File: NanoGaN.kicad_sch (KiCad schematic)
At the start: 11 parts, among them J1 U_DC, J2 GND, J3 Phase_U, J4 Phase_V, J5 Phase_W

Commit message: WiP layout
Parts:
- removed H1, H2, H3, H4, H5, H6: MountingHole, MountingHole:MountingHole_3.2mm_M3, symbol Mechanical:MountingHole
- added FM1, FM2, FM3: Fiducial, Fiducial:Fiducial_1mm_Mask2mm, symbol Mechanical:Fiducial
- added MH1, MH2, MH3, MH4, MH5, MH6: M2, MountingHole:MountingHole_2.2mm_M2_Pad_Via, symbol Mechanical:MountingHole_Pad
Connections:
- new net GND: MH1.1, MH2.1, MH3.1, MH4.1, MH5.1, MH6.1
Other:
- sheet Connectors ports: added SERVO; removed none
- sheet MCU ports: added SERVO; removed none

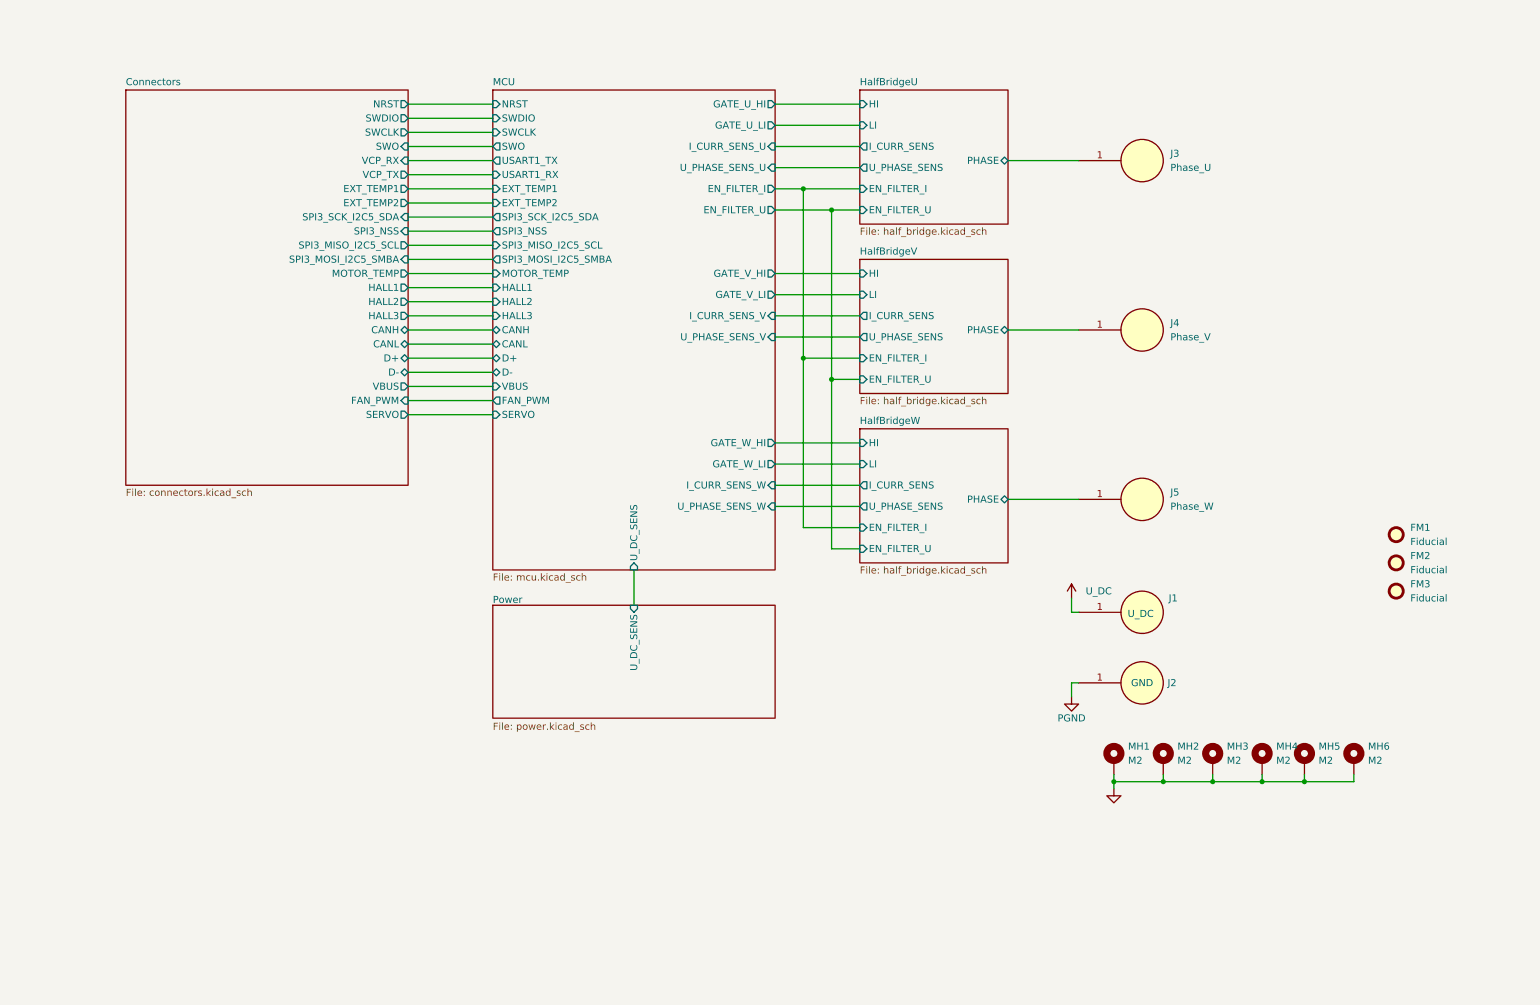
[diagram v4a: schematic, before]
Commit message: added over current protection triggers (adjustable)
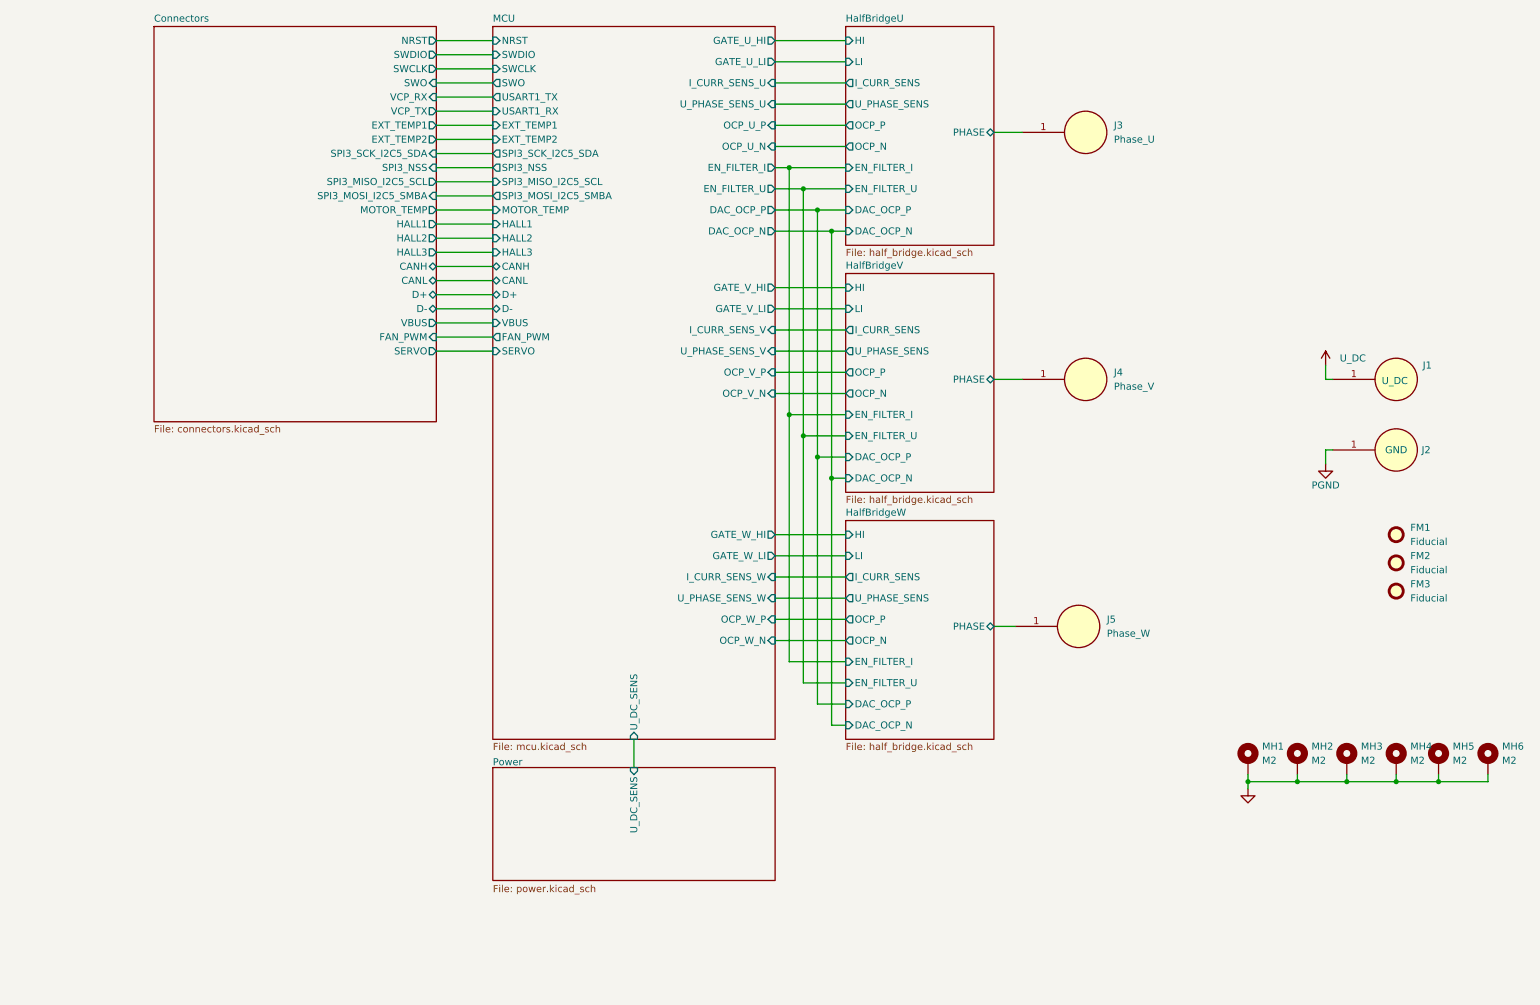
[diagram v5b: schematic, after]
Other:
- sheet HalfBridgeU ports: added DAC_OCP_N, DAC_OCP_P, OCP_N, OCP_P; removed none
- sheet HalfBridgeV ports: added DAC_OCP_N, DAC_OCP_P, OCP_N, OCP_P; removed none
- sheet HalfBridgeW ports: added DAC_OCP_N, DAC_OCP_P, OCP_N, OCP_P; removed none
- sheet MCU ports: added DAC_OCP_N, DAC_OCP_P, OCP_U_N, OCP_U_P, OCP_V_N, OCP_V_P, OCP_W_N, OCP_W_P; removed none
- moved on the sheet: J1, J2, J3, J4, J5, MH1, MH2, MH3, MH4, MH5, MH6

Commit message: WiP layout
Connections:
- net GND: no longer MH3.1, MH4.1, MH5.1, MH6.1
- net PGND: now also MH3.1, MH4.1, MH5.1, MH6.1
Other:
- sheet Connectors ports: added none; removed VBUS
- sheet MCU ports: added none; removed VBUS
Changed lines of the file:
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@@
+	)
+	(junction
+		(at 160.02 58.42)
+		(diameter 0)
+		(color 0 0 0 0)
+	)
+	(junction
+		(at 157.48 99.06)
+		(diameter 0)
+		(color 0 0 0 0)
+	)
+	(junction
+		(at 152.4 91.44)
+		(diameter 0)
+		(color 0 0 0 0)
+	)
+	(junction
+		(at 154.94 95.25)
+		(diameter 0)
+		(color 0 0 0 0)
 	)
 	(junction
@@
 	)
 	(junction
-		(at 160.02 58.42)
-		(diameter 0)
-		(color 0 0 0 0)
-	)
-	(junction
-		(at 157.48 99.06)
-		(diameter 0)
-		(color 0 0 0 0)
-	)
-	(junction
-		(at 152.4 91.44)
-		(diameter 0)
-		(color 0 0 0 0)
-	)
-	(junction
-		(at 154.94 95.25)
-		(diameter 0)
-		(color 0 0 0 0)
-	)
-	(junction
 		(at 269.24 157.48)
 		(diameter 0)
@@
 		(color 0 0 0 0)
 	)
-	(junction
-		(at 243.84 157.48)
-		(diameter 0)
-		(color 0 0 0 0)
-	)
 	(wire
 		(pts
@@
 	(wire
 		(pts
+			(xy 88.9 74.93) (xy 99.06 74.93)
+		)
+		(stroke
+			(width 0)
+			(type default)
+		)
+	)
+	(wire
+		(pts
 			(xy 88.9 72.39) (xy 99.06 72.39)
 		)
@@
 	(wire
 		(pts
-			(xy 88.9 80.01) (xy 99.06 80.01)
+			(xy 88.9 77.47) (xy 99.06 77.47)
 		)
 		(stroke
@@
 	(wire
 		(pts
-			(xy 88.9 77.47) (xy 99.06 77.47)
-		)
-		(stroke
-			(width 0)
-			(type default)
-		)
-	)
-	(wire
-		(pts
 			(xy 149.86 27.94) (xy 162.56 27.94)
 		)
@@
 	(wire
 		(pts
+			(xy 252.73 157.48) (xy 252.73 158.75)
+		)
+		(stroke
+			(width 0)
+			(type default)
+		)
+	)
+	(wire
+		(pts
 			(xy 162.56 99.06) (xy 157.48 99.06)
 		)
@@
 	(wire
 		(pts
-			(xy 88.9 74.93) (xy 99.06 74.93)
-		)
-		(stroke
-			(width 0)
-			(type default)
-		)
-	)
-	(wire
-		(pts
 			(xy 160.02 147.32) (xy 160.02 102.87)
 		)
@@
 		(pts
 			(xy 248.92 97.79) (xy 248.92 100.33)
-		)
-		(stroke
-			(width 0)
-			(type default)
-		)
-	)
-	(wire
-		(pts
-			(xy 252.73 157.48) (xy 243.84 157.48)
 		)
 		(stroke
@@
 					(size 1.27 1.27)
 				)
-				(hide yes)
 			)
 		)
@@
 				(path "/aa8a494f-605e-4a00-9d3c-daec94709fcb"
 					(reference "#PWR0131")
+					(unit 1)
+				)
+			)
+		)
+	)
+	(symbol
+		(lib_id "power:GND")
+		(at 252.73 158.75 0)
+		(unit 1)
+		(exclude_from_sim no)
+		(in_bom yes)
+		(on_board yes)
+		(dnp no)
+		(property "Reference" "#PWR0111"
+			(at 252.73 165.1 0)
+			(effects
+				(font
+					(size 1.27 1.27)
+				)
+				(hide yes)
+			)
+		)
+		(property "Value" "PGND"
+			(at 252.73 162.814 0)
+			(effects
+				(font
+					(size 1.27 1.27)
+				)
+			)
+		)
+		(property "Footprint" ""
+			(at 252.73 158.75 0)
+			(effects
+				(font
+					(size 1.27 1.27)
+				)
+				(hide yes)
+			)
+		)
+		(property "Datasheet" ""
+			(at 252.73 158.75 0)
+			(effects
+				(font
+					(size 1.27 1.27)
+				)
+				(hide yes)
+			)
+		)
+		(property "Description" "Power symbol creates a global label with name \"GND\" , ground"
+			(at 252.73 158.75 0)
+			(effects
+				(font
+					(size 1.27 1.27)
+				)
+				(hide yes)
+			)
+		)
+		(pin "1"
+		)
+		(instances
+			(project "NanoGaN"
+				(path "/aa8a494f-605e-4a00-9d3c-daec94709fcb"
+					(reference "#PWR0111")
 					(unit 1)
 				)
@@
 			)
 		)
-		(pin "VBUS" output
-			(at 88.9 74.93 0)
-			(effects
-				(font
-					(size 1.27 1.27)
-				)
-				(justify right)
-			)
-		)
 		(pin "EXT_TEMP1" output
 			(at 88.9 39.37 0)
@@
 		)
 		(pin "FAN_PWM" input
+			(at 88.9 74.93 0)
+			(effects
+				(font
+					(size 1.27 1.27)
+				)
+				(justify right)
+			)
+		)
+		(pin "SERVO" output
 			(at 88.9 77.47 0)
-			(effects
-				(font
-					(size 1.27 1.27)
-				)
-				(justify right)
-			)
-		)
-		(pin "SERVO" output
-			(at 88.9 80.01 0)
 			(effects
 				(font
@@
 			)
 		)
-		(pin "VBUS" input
-			(at 99.06 74.93 180)
-			(effects
-				(font
-					(size 1.27 1.27)
-				)
-				(justify left)
-			)
-		)
 		(pin "D-" bidirectional
 			(at 99.06 72.39 180)
@@
 		)
 		(pin "FAN_PWM" output
+			(at 99.06 74.93 180)
+			(effects
+				(font
+					(size 1.27 1.27)
+				)
+				(justify left)
+			)
+		)
+		(pin "SERVO" input
 			(at 99.06 77.47 180)
 			(effects
 				(font
-					(size 1.27 1.27)
-				)
-				(justify left)
-			)
-		)
-		(pin "SERVO" input
-			(at 99.06 80.01 180)
-			(effects
-				(font

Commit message: added the first draft of the layout
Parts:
- removed J1: U_DC, TerminalBlock_Wuerth:Wuerth_REDCUBE-THR_WP-THRBU_74650073_THR, symbol Connector_Generic:Power_Welding_PAD
- removed J2: GND, TerminalBlock_Wuerth:Wuerth_REDCUBE-THR_WP-THRBU_74650073_THR, symbol Connector_Generic:Power_Welding_PAD
- added CC1: ~, NanoGaN:CoolingChannel, symbol NanoGaN:CoolingChannel
- added J1, J2: XT60-M, NanoGaN:AMASS_XT60-M, symbol NanoGaN:XT60-M
- added MH7: M3, MountingHole:MountingHole_3.2mm_M3_Pad_Via, symbol Mechanical:MountingHole_Pad
- MH1, MH2, MH3, MH4, MH5, MH6: value M2 -> M3; footprint MountingHole:MountingHole_2.2mm_M2_Pad_Via -> MountingHole:MountingHole_3.2mm_M3_Pad_Via
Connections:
- net GND: now also MH3.1
- net PGND: now also J1.N (NEG), J2.N (NEG), MH7.1; no longer MH3.1
- net U_DC: now also J1.P (POS), J2.P (POS)
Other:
- sheet HalfBridgeU ports: added I_CURR_SENS+, I_CURR_SENS-; removed EN_FILTER_I, EN_FILTER_U, I_CURR_SENS
- sheet HalfBridgeV ports: added I_CURR_SENS+, I_CURR_SENS-; removed EN_FILTER_I, EN_FILTER_U, I_CURR_SENS
- sheet HalfBridgeW ports: added I_CURR_SENS+, I_CURR_SENS-; removed EN_FILTER_I, EN_FILTER_U, I_CURR_SENS
- sheet MCU ports: added I_CURR_SENS_U+, I_CURR_SENS_U-, I_CURR_SENS_V+, I_CURR_SENS_V-, I_CURR_SENS_W+, I_CURR_SENS_W-; removed EN_FILTER_I, EN_FILTER_U, I_CURR_SENS_U, I_CURR_SENS_V, I_CURR_SENS_W
- note added: "Mechanical Stuff (no BOM)"
- moved on the sheet: FM1, FM2, FM3, MH1

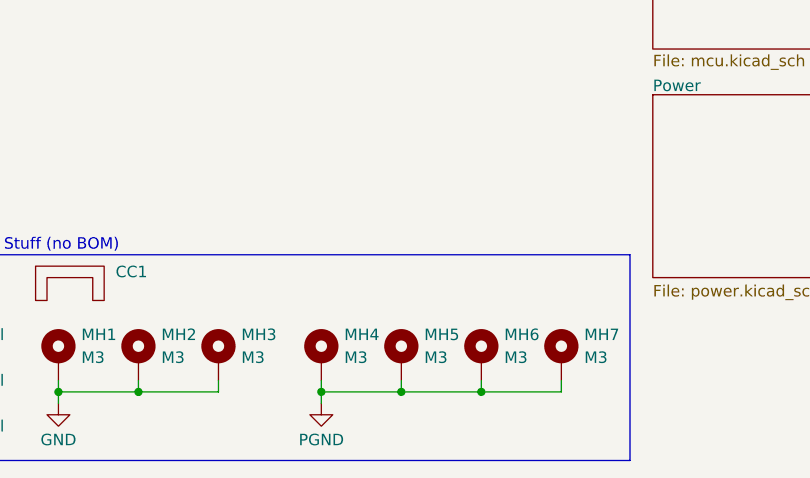
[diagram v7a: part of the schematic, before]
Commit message: added heatsinks and updated cooling channel
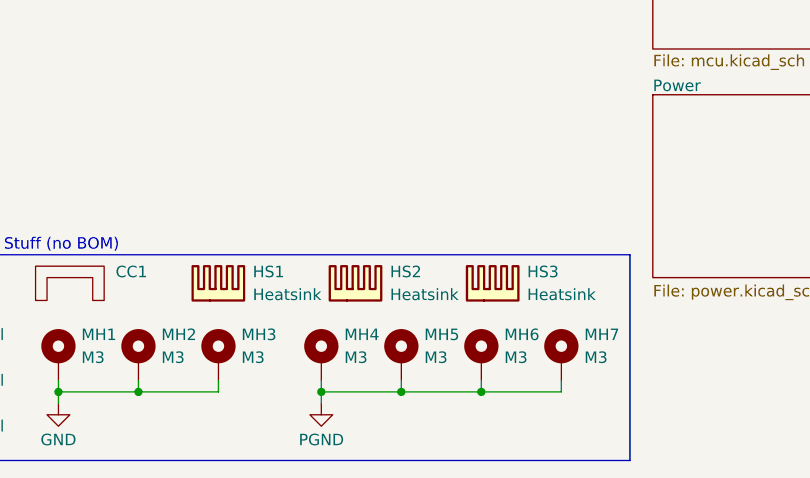
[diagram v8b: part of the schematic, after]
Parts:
- added HS1, HS2, HS3: Heatsink, NanoGaN:HSB01-080808, symbol Mechanical:Heatsink
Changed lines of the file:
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@@
+	)
+	(symbol
+		(lib_id "Mechanical:Heatsink")
+		(at 66.04 177.8 0)
+		(unit 1)
+		(exclude_from_sim no)
+		(in_bom yes)
+		(on_board yes)
+		(dnp no)
+		(fields_autoplaced yes)
+		(property "Reference" "HS2"
+			(at 69.85 174.6249 0)
+			(effects
+				(font
+					(size 1.27 1.27)
+				)
+				(justify left)
+			)
+		)
+		(property "Value" "Heatsink"
+			(at 69.85 177.1649 0)
+			(effects
+				(font
+					(size 1.27 1.27)
+				)
+				(justify left)
+			)
+		)
+		(property "Footprint" "NanoGaN:HSB01-080808"
+			(at 66.3448 177.8 0)
+			(effects
+				(font
+					(size 1.27 1.27)
+				)
+				(hide yes)
+			)
+		)
+		(property "Datasheet" "~"
+			(at 66.3448 177.8 0)
+			(effects
+				(font
+					(size 1.27 1.27)
+				)
+				(hide yes)
+			)
+		)
+		(property "Description" "Heatsink"
+			(at 66.04 177.8 0)
+			(effects
+				(font
+					(size 1.27 1.27)
+				)
+				(hide yes)
+			)
+		)
+		(instances
+			(project "NanoGaN"
+				(path "/aa8a494f-605e-4a00-9d3c-daec94709fcb"
+					(reference "HS2")
+					(unit 1)
+				)
+			)
+		)
+	)
+	(symbol
+		(lib_id "Mechanical:Heatsink")
+		(at 81.28 177.8 0)
+		(unit 1)
+		(exclude_from_sim no)
+		(in_bom yes)
+		(on_board yes)
+		(dnp no)
+		(fields_autoplaced yes)
+		(property "Reference" "HS3"
+			(at 85.09 174.6249 0)
+			(effects
+				(font
+					(size 1.27 1.27)
+				)
+				(justify left)
+			)
+		)
+		(property "Value" "Heatsink"
+			(at 85.09 177.1649 0)
+			(effects
+				(font
+					(size 1.27 1.27)
+				)
+				(justify left)
+			)
+		)
+		(property "Footprint" "NanoGaN:HSB01-080808"
+			(at 81.5848 177.8 0)
+			(effects
+				(font
+					(size 1.27 1.27)
+				)
+				(hide yes)
+			)
+		)
+		(property "Datasheet" "~"
+			(at 81.5848 177.8 0)
+			(effects
+				(font
+					(size 1.27 1.27)
+				)
+				(hide yes)
+			)
+		)
+		(property "Description" "Heatsink"
+			(at 81.28 177.8 0)
+			(effects
+				(font
+					(size 1.27 1.27)
+				)
+				(hide yes)
+			)
+		)
+		(instances
+			(project "NanoGaN"
+				(path "/aa8a494f-605e-4a00-9d3c-daec94709fcb"
+					(reference "HS3")
+					(unit 1)
+				)
+			)
+		)
 	)
 	(symbol
@@
 					(unit 1)
 				)
+			)
+		)
+	)
+	(symbol
+		(lib_id "Mechanical:Heatsink")
+		(at 50.8 177.8 0)
+		(unit 1)
+		(exclude_from_sim no)
+		(in_bom yes)
+		(on_board yes)
+		(dnp no)
+		(fields_autoplaced yes)
+		(property "Reference" "HS1"
+			(at 54.61 174.6249 0)
+			(effects
+				(font
+					(size 1.27 1.27)
+				)
+				(justify left)
+			)
+		)
+		(property "Value" "Heatsink"
+			(at 54.61 177.1649 0)
+			(effects
+				(font
+					(size 1.27 1.27)
+				)
+				(justify left)
+			)
+		)
+		(property "Footprint" "NanoGaN:HSB01-080808"
+			(at 51.1048 177.8 0)
+			(effects
+				(font
+					(size 1.27 1.27)
+				)
+				(hide yes)
+			)
+		)
+		(property "Datasheet" "~"
+			(at 51.1048 177.8 0)
+			(effects
+				(font
+					(size 1.27 1.27)
+				)
+				(hide yes)
+			)
+		)
+		(property "Description" "Heatsink"
+			(at 50.8 177.8 0)
+			(effects
+				(font
+					(size 1.27 1.27)
+				)
+				(hide yes)
+			)
+		)
+		(instances
+			(project ""
+				(path "/aa8a494f-605e-4a00-9d3c-daec94709fcb"
+					(reference "HS1")
+					(unit 1)
+				)
